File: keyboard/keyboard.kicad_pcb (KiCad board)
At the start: 2 copper layers, 106.5 x 124 mm, 84 parts, among them J2 Conn_01x04, SW1 SW_Push, SW10 SW_Push, SW11 SW_Push, SW12 SW_Push, SW13 SW_Push, SW14 SW_Push, SW15 SW_Push, SW16 SW_Push, SW17 SW_Push, SW2 SW_Push, SW21 SW_Push, SW3 SW_Push, SW4 SW_Push, SW5 SW_Push, SW6 SW_Push, SW7 SW_Push, SW8 SW_Push, SW9 SW_Push, U1 AP2127K-3.3, U2 USBLC6-2SC6, U3 STM32F072CBTx

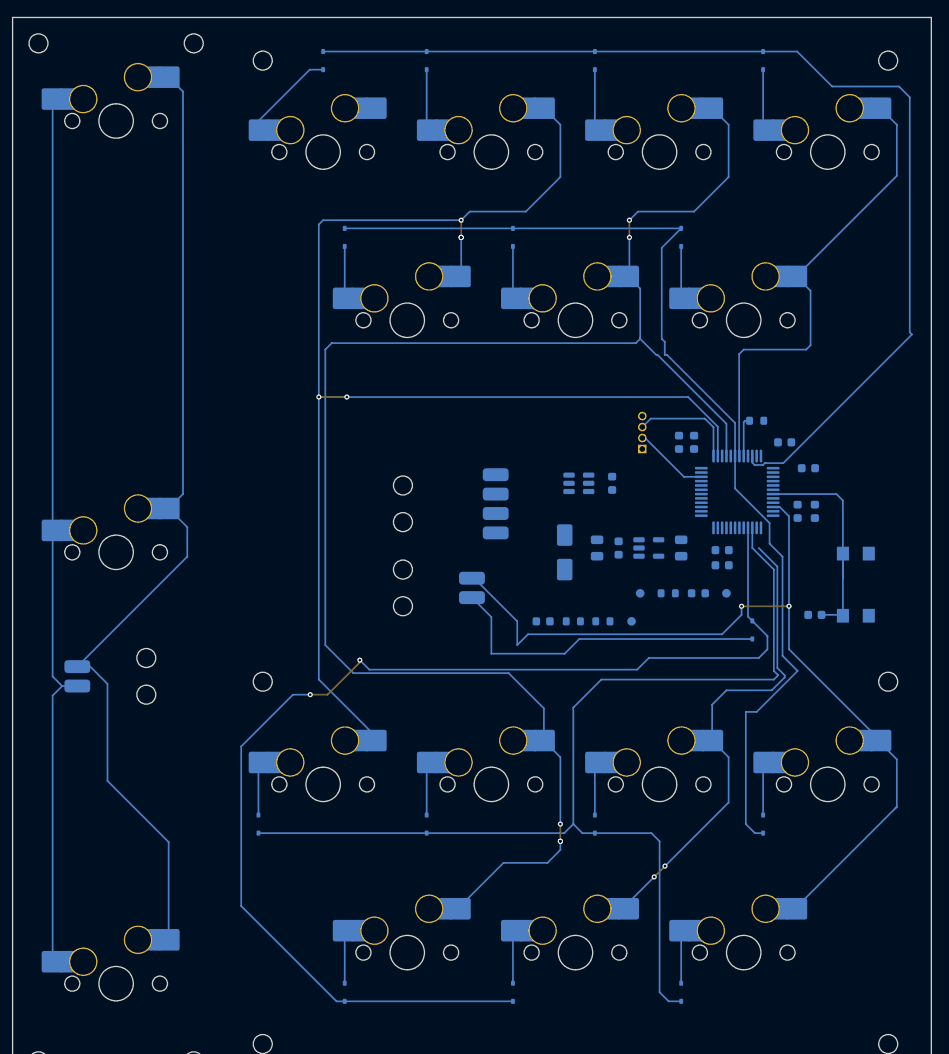
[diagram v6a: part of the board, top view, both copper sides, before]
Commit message: Delete traces and vias before new layout.
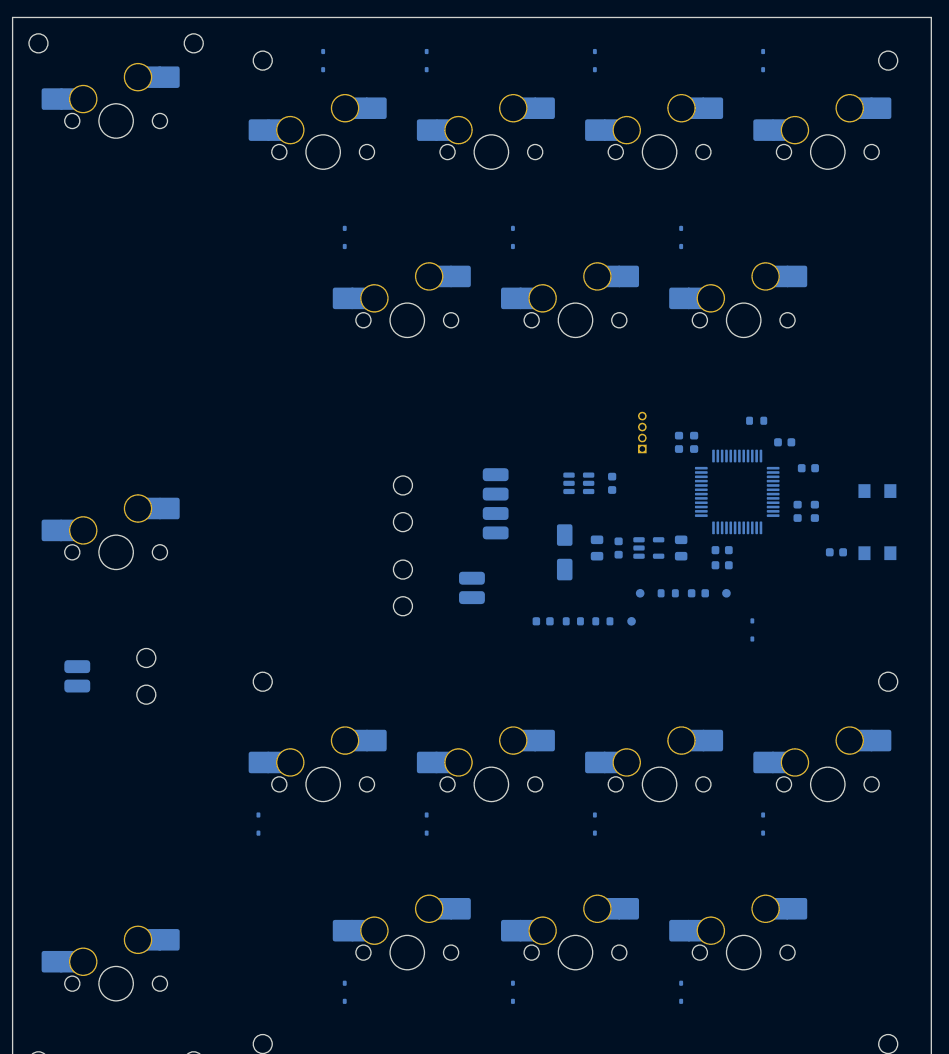
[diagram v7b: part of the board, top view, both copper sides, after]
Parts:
- moved C5 7.67 mm to (178.5, 97.0)
- moved SW21 7.67 mm to (183.2, 93.5)
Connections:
- D18 pad 2: /SB_1 -> Net-(D18-A)
- SW15 pad 1: /SB_1 -> Net-(J3-Pin_1)
- SW16 pad 1: /SB_1 -> Net-(J3-Pin_1)
- SW17 pad 1: /SB_1 -> Net-(J3-Pin_1)
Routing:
- net /COL3: track 215.9 -> 0.00 mm, vias 2 -> 0
- net /COL1: track 185.8 -> 0.00 mm, vias 5 -> 0
- net /COL2: track 159.4 -> 0.00 mm, vias 5 -> 0
- net /SB_1: track 141.1 -> 0.00 mm
- net /ROW3: track 136.3 -> 0.00 mm, vias 2 -> 0
- net /ROW2: track 125.3 -> 0.00 mm
- net /ROW0: track 123.4 -> 0.00 mm
- net /ROW1: track 121.3 -> 0.00 mm
- net /COL0: track 109.5 -> 0.00 mm, vias 2 -> 0
- net /NRST: track 27.1 -> 0.00 mm
- net /SWCLK: track 12.4 -> 0.00 mm
- net Net-(D7-A): track 11.0 -> 0.00 mm
- net /SWDIO: track 8.70 -> 0.00 mm
- net Net-(D6-A): track 7.07 -> 0.00 mm
- net Net-(D5-A): track 7.07 -> 0.00 mm
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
